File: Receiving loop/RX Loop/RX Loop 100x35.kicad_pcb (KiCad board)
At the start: 2 copper layers, 100 x 35 mm, 40 parts, among them IC1 GALI-74, IC2 GALI-74, J1 VCC, K1 G5V-1, K2 G5V-1, T1 Fair-Rite 2873000202, U1 L7812

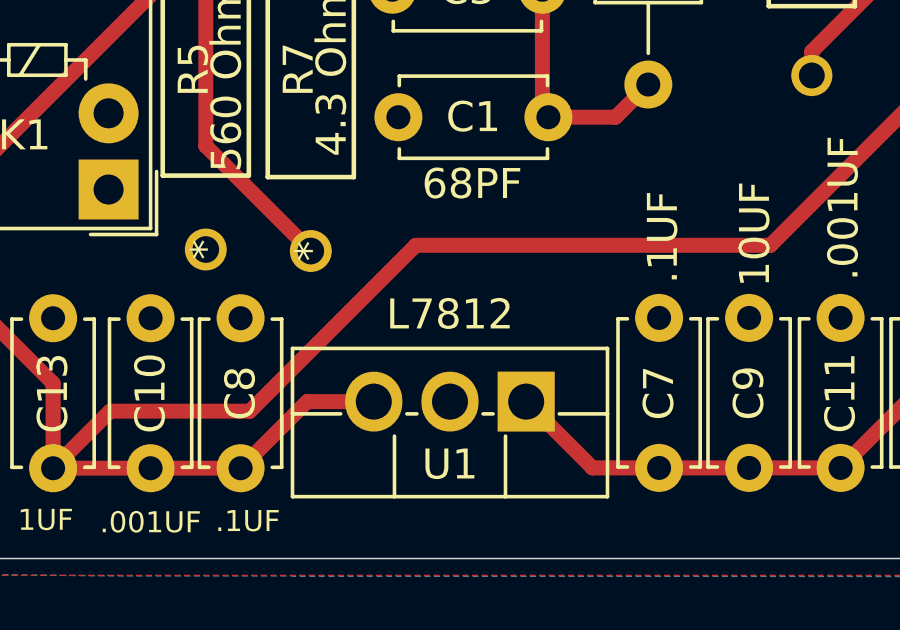
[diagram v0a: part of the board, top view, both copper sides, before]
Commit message: Fixed footprint label for U1
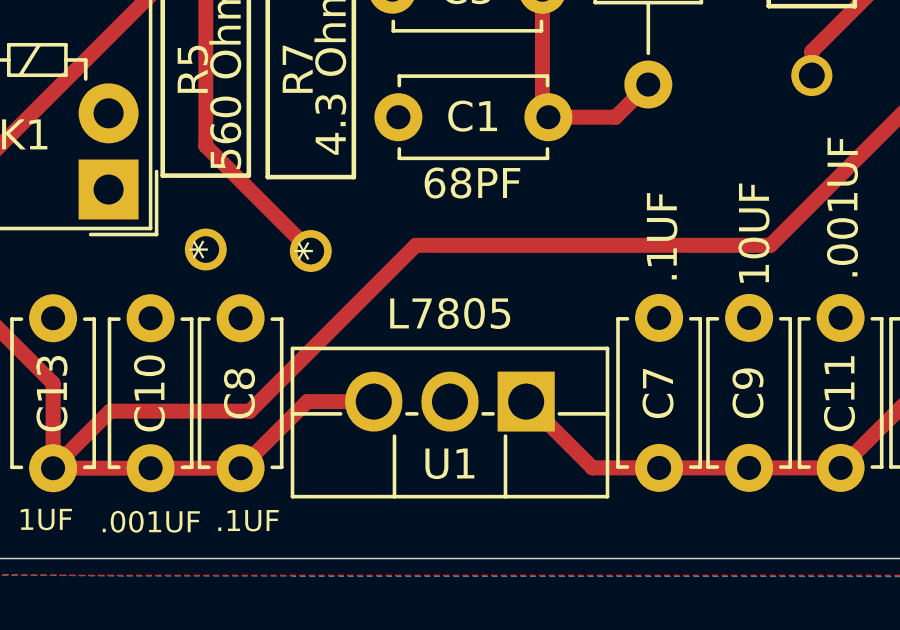
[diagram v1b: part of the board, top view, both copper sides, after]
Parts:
- U1: value L7812 -> L7805

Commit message: Updated PCB
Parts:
- U1: value L7805 -> L7812
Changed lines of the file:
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@@
   (page A4)
   (layers
-    (0 F.Cu signal hide)
+    (0 F.Cu signal)
     (31 B.Cu signal)
     (32 B.Adhes user)
@@
       (effects (font (size 1 1) (thickness 0.15)))
     )
-    (fp_text value L7805 (at 2.54 2.9025) (layer F.SilkS)
+    (fp_text value L7812 (at 2.54 2.9025) (layer F.SilkS)
       (effects (font (size 1 1) (thickness 0.15)))
     )

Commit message: Updating changes. Cleaning up repo.wq
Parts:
- U1: value L7812 -> L7809

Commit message: Merged changes.
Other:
- board text added: "RX Loop Amplifier Rev: 20210620"
- board text removed: "RX Loop Amplifier Rev: 20210314"
